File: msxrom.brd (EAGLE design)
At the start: 100 x 80 mm, 9 parts

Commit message: with io breakout
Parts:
- added JP10, JP11, JP12, JP13, JP15, JP16: (no value), pinhead-round:1X01
- added JP14, JP17, JP18, JP9: (no value), pinhead-round:1X04
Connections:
- new net !IORQ: JP1./IORQ, JP11.1
- new net !RD: JP1./RD, JP13.1, JP16.1
- new net !WAIT: JP1./WAIT, JP10.1
- new net !WR: JP1./WR, JP12.1, JP15.1
- new net N$9: JP1.SW1, JP1.SW2
- net A0: now also JP17.1
- net A1: now also JP17.2
- net A2: now also JP17.3
- net N$1: now also JP9.1
- net N$13: now also JP18.4
- net N$14: now also JP18.3
- net N$15: now also JP18.2
- net N$16: now also JP18.1
- net N$17: now also JP17.4
- net N$2: now also JP9.2
- net N$3: now also JP9.3
- net N$4: now also JP9.4
- net N$5: now also JP14.1
- net N$6: now also JP14.2
- net N$7: now also JP14.3
- net N$8: now also JP14.4
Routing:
- net !WR: track 0.00 -> 105.7 mm, vias 0 -> 3
- net !RD: track 0.00 -> 104.4 mm, vias 0 -> 2
- net !IORQ: track 0.00 -> 103.4 mm, vias 0 -> 2
- net !WAIT: track 0.00 -> 74.0 mm, vias 0 -> 2
- net N$13: track 45.0 -> 91.7 mm, vias 1 -> 2
- net N$14: track 55.1 -> 98.6 mm, vias 4 -> 5
- net N$15: track 54.4 -> 94.7 mm, vias 3 -> 4
- net N$16: track 50.1 -> 87.1 mm, vias 2 -> 3
- net N$17: track 46.8 -> 81.5 mm, vias 3 -> 4
- net A2: track 42.4 -> 75.2 mm, vias 2 -> 3
- net A1: track 39.2 -> 70.1 mm, vias 1 -> 2
- net N$1: track 39.9 -> 70.4 mm, vias 2 -> 4
- net N$4: track 27.2 -> 56.9 mm
- net N$6: track 27.2 -> 56.9 mm
- net N$5: track 22.9 -> 52.6 mm
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- added copper zone on layer 16, net GND

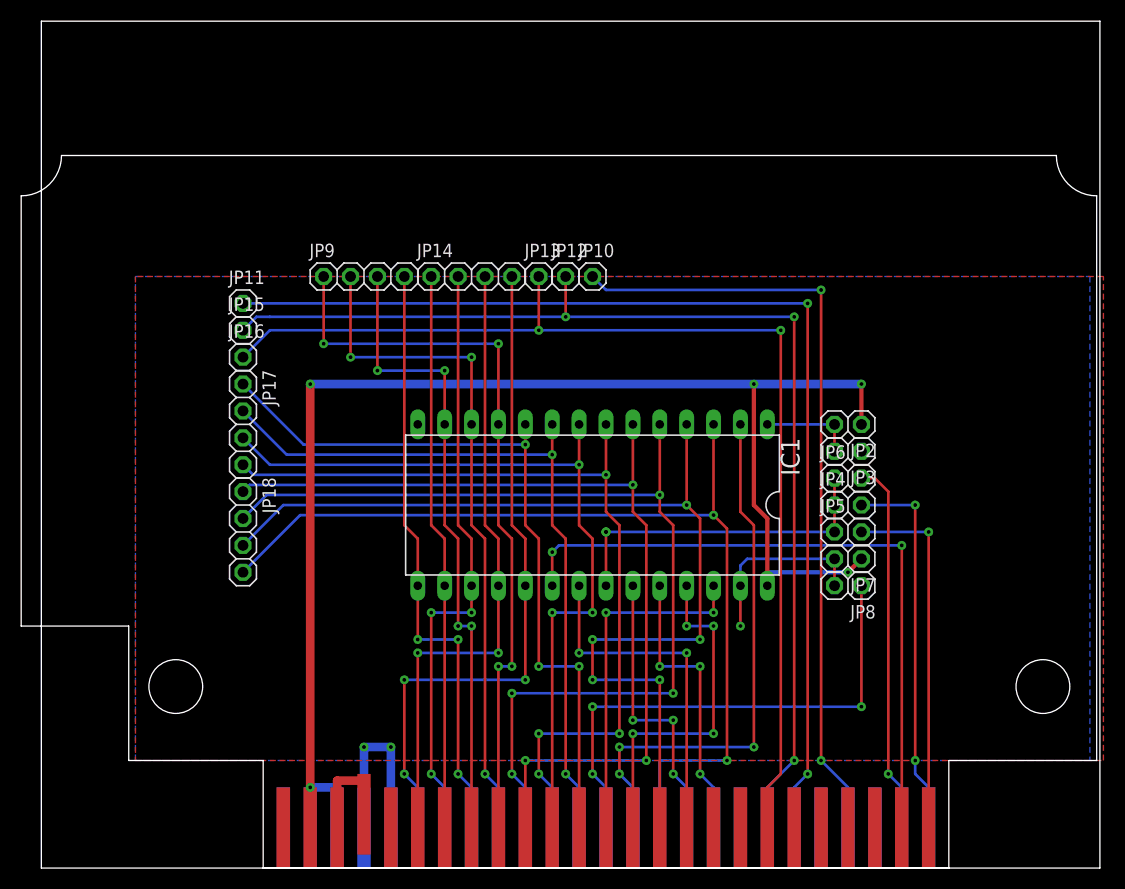
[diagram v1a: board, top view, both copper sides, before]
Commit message: finished board but eagle broke something...
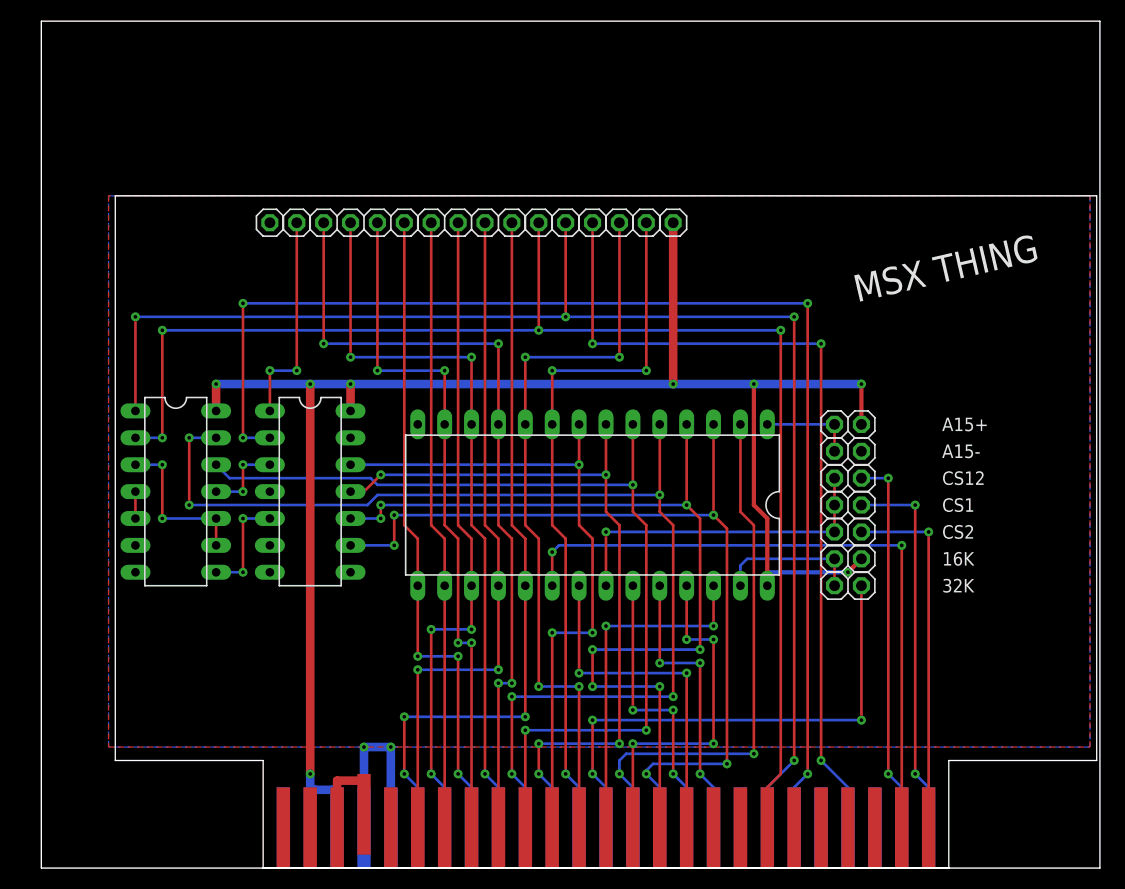
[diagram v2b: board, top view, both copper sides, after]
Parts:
- removed JP11, JP15, JP16: (no value), pinhead-round:1X01
- removed JP17, JP18: (no value), pinhead-round:1X04
- added A15+, A15-, CS1, CS12, CS2: (no value), pinhead-round:1X02
- added V1: 74HCT00N, 74ttl-din:DIL14
- added V2: 744078N, 74ttl-din:DIL14
- JP2, JP3, JP4, JP5, JP6: device pinhead-round:1X02 -> pinhead-round:1X01
- moved JP5 61.9 mm to (21.6, 61.0)
- moved JP2 55.4 mm to (24.1, 61.0), turned to 0 degrees
- moved JP4 32.8 mm to (57.1, 61.0)
- moved JP3 30.5 mm to (54.6, 61.0), turned to 0 degrees
- moved JP6 29.2 mm to (59.7, 61.0)
- moved JP10 5.08 mm to (52.1, 61.0)
- moved JP12 5.08 mm to (49.5, 61.0)
- moved JP13 5.08 mm to (47.0, 61.0)
- moved JP14 5.08 mm to (40.6, 61.0)
- moved JP9 5.08 mm to (30.5, 61.0)
- renumbered JP7 to 16K, JP8 to 32K
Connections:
- removed net N$13: IC1.3, JP1.A7, JP18.4
- removed net N$14: IC1.4, JP1.A6, JP18.3
- removed net N$15: IC1.5, JP1.A5, JP18.2
- removed net N$16: IC1.6, JP1.A4, JP18.1
- removed net N$17: IC1.7, JP1.A3, JP17.4
- new net !A4A5: V1.11, V2.3
- new net !IOSEL: JP2.1, V2.1
- new net !RW: V1.8, V2.5
- new net A3: IC1.7, JP1.A3, V2.11
- new net A4: IC1.6, JP1.A4, V1.12
- new net A5: IC1.5, JP1.A5, V1.13
- new net A6: IC1.4, JP1.A6, V2.10
- new net A7: IC1.3, JP1.A7, V2.9
- new net N$10: V1.10, V1.3, V1.9
- net !CS1: now also CS1.2; no longer JP4.2
- net !CS12: now also CS12.2; no longer JP6.2
- net !CS2: now also CS2.2; no longer JP5.2
- net !IORQ: now also V2.2; no longer JP11.1
- net !OE: now also CS1.1, CS12.1, CS2.1; no longer JP4.1, JP5.1, JP6.1
- net !RD: now also V1.2; no longer JP16.1
- net !WR: now also V1.1; no longer JP15.1
- net A0: now also JP3.1; no longer JP17.1
- net A1: now also JP4.1; no longer JP17.2
- net A15: now also A15+.2, A15-.2; no longer JP2.2, JP3.2
- net A2: now also V2.12; no longer JP17.3
- net GND: now also A15-.1, JP5.1, V1.4, V1.5, V1.7, V2.4, V2.7; no longer JP3.1
- net VCC: now also A15+.1, JP6.1, V1.14, V2.14; no longer JP2.1
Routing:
- net A5: track 0.00 -> 108.1 mm, vias 0 -> 6
- net N$14: track 98.6 -> 0.00 mm, vias 5 -> 0
- net N$15: track 94.7 -> 0.00 mm, vias 4 -> 0
- net N$13: track 91.7 -> 0.00 mm, vias 2 -> 0
- net A4: track 0.00 -> 90.2 mm, vias 0 -> 3
- net A6: track 0.00 -> 88.2 mm, vias 0 -> 7
- net N$16: track 87.1 -> 0.00 mm, vias 3 -> 0
- net A7: track 0.00 -> 83.5 mm, vias 0 -> 5
- net N$17: track 81.5 -> 0.00 mm, vias 4 -> 0
- net A3: track 0.00 -> 71.6 mm, vias 0 -> 5
- net VCC: track 134.4 -> 167.3 mm, vias 5 -> 8
- net !RD: track 104.4 -> 128.8 mm, vias 2 -> 4
- net !WR: track 105.7 -> 129.3 mm, vias 3 -> 4
- net !IOSEL: track 0.00 -> 20.3 mm, vias 0 -> 2
- net !IORQ: track 103.4 -> 118.6 mm, vias 2 -> 4
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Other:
- board text added: "MSX THING"

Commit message: with sdx connector and branding
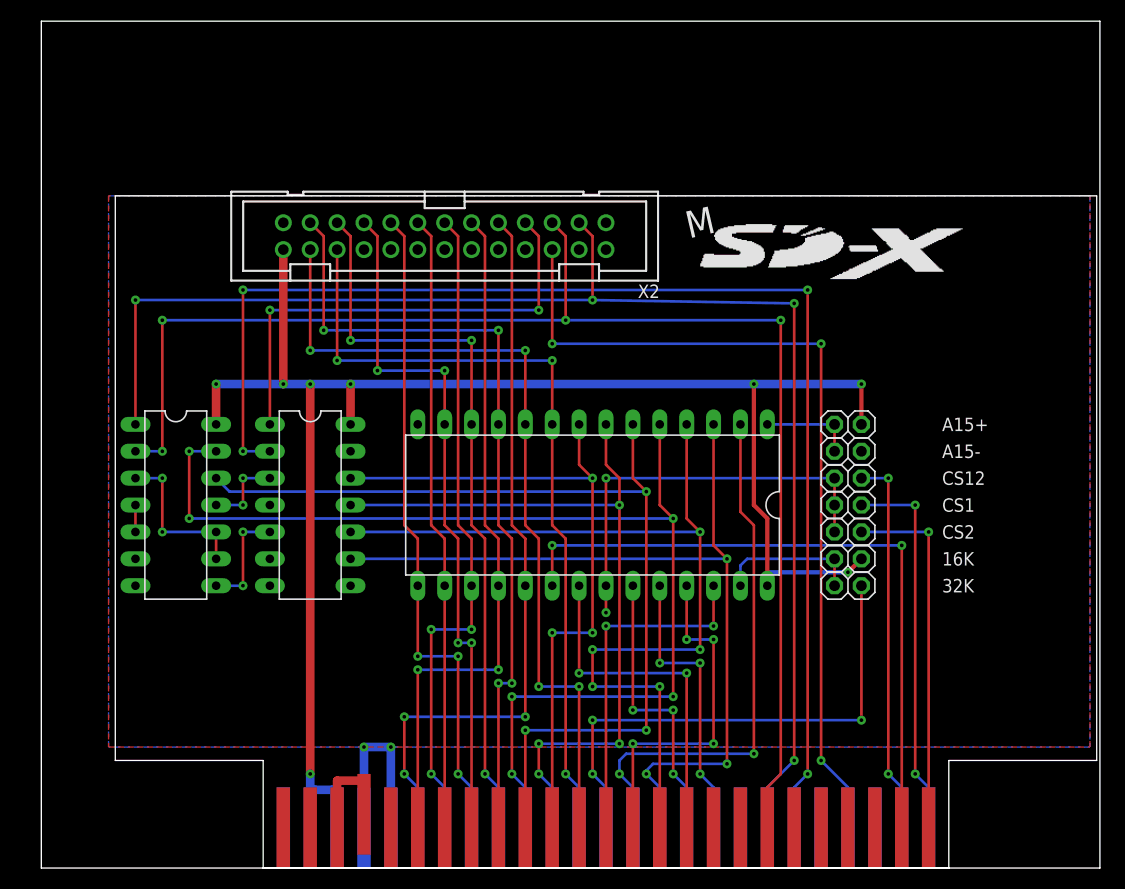
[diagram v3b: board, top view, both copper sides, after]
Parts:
- removed JP10, JP12, JP13, JP2, JP3, JP4, JP5, JP6: (no value), pinhead-round:1X01
- removed JP14, JP9: (no value), pinhead-round:1X04
- added X2: 2526-, con-3m:PAK100/2500-26
- moved V1 1.27 mm to (12.7, 34.3)
- moved V2 1.27 mm to (25.4, 34.3)
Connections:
- removed net N$1: IC1.11, JP1.D0, JP9.1
- removed net N$2: IC1.12, JP1.D1, JP9.2
- removed net N$3: IC1.13, JP1.D2, JP9.3
- removed net N$4: IC1.15, JP1.D3, JP9.4
- removed net N$5: IC1.16, JP1.D4, JP14.1
- removed net N$6: IC1.17, JP1.D5, JP14.2
- removed net N$7: IC1.18, JP1.D6, JP14.3
- removed net N$8: IC1.19, JP1.D7, JP14.4
- new net !RESET: X2.8
- new net D0: IC1.11, JP1.D0, X2.23
- new net D1: IC1.12, JP1.D1, X2.21
- new net D2: IC1.13, JP1.D2, X2.19
- new net D3: IC1.15, JP1.D3, X2.17
- new net D4: IC1.16, JP1.D4, X2.15
- new net D5: IC1.17, JP1.D5, X2.13
- new net D6: IC1.18, JP1.D6, X2.11
- new net D7: IC1.19, JP1.D7, X2.9
- new net RX-S: X2.4
- new net TX-S: X2.2
- net !IOSEL: now also X2.7; no longer JP2.1
- net !RD: now also X2.5; no longer JP13.1
- net !WAIT: now also X2.6; no longer JP10.1
- net !WR: now also X2.3; no longer JP12.1
- net A0: now also X2.24; no longer JP3.1
- net A1: now also X2.22; no longer JP4.1
- net GND: now also X2.1; no longer JP5.1
- net VCC: now also X2.26; no longer JP6.1
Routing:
- net D0: track 0.00 -> 76.0 mm, vias 0 -> 4
- net N$1: track 75.5 -> 0.00 mm, vias 4 -> 0
- net D7: track 0.00 -> 70.2 mm, vias 0 -> 3
- net D1: track 0.00 -> 70.2 mm, vias 0 -> 3
- net N$2: track 69.6 -> 0.00 mm, vias 3 -> 0
- net N$8: track 69.6 -> 0.00 mm, vias 3 -> 0
- net D6: track 0.00 -> 65.8 mm, vias 0 -> 2
- net D2: track 0.00 -> 65.8 mm, vias 0 -> 4
- net N$3: track 65.3 -> 0.00 mm, vias 4 -> 0
- net N$7: track 65.3 -> 0.00 mm, vias 2 -> 0
- net D5: track 0.00 -> 62.5 mm, vias 0 -> 3
- net D3: track 0.00 -> 62.5 mm, vias 0 -> 3
- net N$6: track 62.0 -> 0.00 mm, vias 3 -> 0
- net N$4: track 62.0 -> 0.00 mm, vias 3 -> 0
- net D4: track 0.00 -> 58.2 mm
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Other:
- board text added: "M"
- board text removed: "MSX THING"

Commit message: msxrom as produced
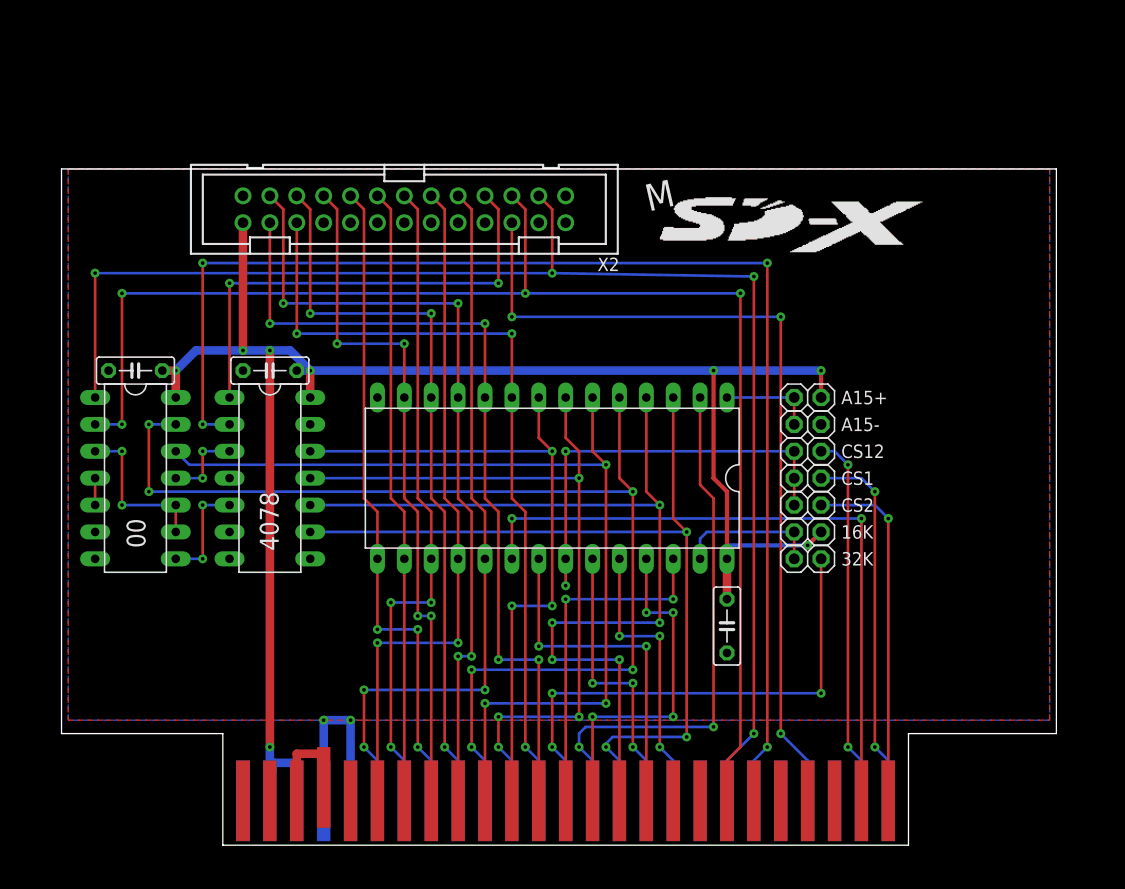
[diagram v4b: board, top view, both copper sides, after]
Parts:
- added C1, C2, C3: (no value), rcl:C050-025X075
- moved A15+ 4.58 mm to (72.4, 44.5)
- moved 16K 4.58 mm to (72.4, 31.8)
- moved 32K 4.58 mm to (72.4, 29.2)
- moved A15- 4.58 mm to (72.4, 41.9)
- moved CS1 4.58 mm to (72.4, 36.8)
- moved CS12 4.58 mm to (72.4, 39.4)
- moved CS2 4.58 mm to (72.4, 34.3)
- moved IC1 4.58 mm to (48.3, 36.8)
- moved JP1 4.58 mm to (45.7, 43.2)
- moved X2 4.58 mm to (34.3, 62.2)
- moved V1 4.58 mm to (8.89, 36.8)
- moved V2 4.58 mm to (21.6, 36.8)
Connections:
- net GND: now also C1.2, C2.2, C3.2
- net VCC: now also C1.1, C2.1, C3.1
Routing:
- net VCC: track 167.3 -> 170.1 mm
- net !CS12: track 36.1 -> 35.3 mm
- net !CS2: track 34.3 -> 33.5 mm
- net !CS1: track 36.1 -> 35.3 mm
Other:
- board size 100 x 80 mm -> 94 x 63.9 mm
- board text added: "00"
- board text added: "4078"

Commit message: loose files
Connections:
- removed net !IOSEL: V2.1, X2.7
- new net IOSEL: V2.13, X2.7
- net !RESET: now also JP1./RESET
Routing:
- net !RESET: track 0.00 -> 112.3 mm, vias 0 -> 5
- net !IOSEL: track 45.0 -> 0.00 mm, vias 2 -> 0
- net IOSEL: track 0.00 -> 40.9 mm, vias 0 -> 2
- net !OE: track 39.4 -> 36.8 mm, vias 2 -> 1
- net VCC: vias 8 -> 6
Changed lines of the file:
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@@
 <contactref element="V2" pad="14"/>
 <wire x1="21.59" y1="48.895" x2="19.05" y2="48.895" width="0.8128" layer="16"/>
-<via x="12.7" y="46.99" extent="1-16" drill="0.35"/>
 <wire x1="19.05" y1="48.895" x2="14.605" y2="48.895" width="0.8128" layer="16"/>
 <wire x1="14.605" y1="48.895" x2="12.7" y2="46.99" width="0.8128" layer="16"/>
-<wire x1="12.7" y1="46.99" x2="12.7" y2="44.45" width="0.8128" layer="1"/>
-<wire x1="25.4" y1="44.45" x2="25.4" y2="46.99" width="0.8128" layer="1"/>
-<via x="25.4" y="46.99" extent="1-16" drill="0.35"/>
+<wire x1="12.7" y1="46.99" x2="12.7" y2="44.45" width="0.8128" layer="16"/>
+<wire x1="25.4" y1="44.45" x2="25.4" y2="46.99" width="0.8128" layer="16"/>
 <via x="21.59" y="11.43" extent="1-16" drill="0.35"/>
 <wire x1="24.13" y1="6.35" x2="23.9014" y2="6.1214" width="0.8128" layer="16"/>
@@
 <contactref element="C3" pad="1"/>
 <wire x1="64.77" y1="29.21" x2="64.77" y2="25.4" width="0.8128" layer="1"/>
-<wire x1="11.43" y1="46.99" x2="12.7" y2="46.99" width="0.8128" layer="1"/>
+<wire x1="11.43" y1="46.99" x2="12.7" y2="46.99" width="0.8128" layer="16"/>
 <wire x1="24.13" y1="46.99" x2="25.4" y2="46.99" width="0.8128" layer="16"/>
 </signal>
@@
 <contactref element="CS2" pad="1"/>
 <contactref element="CS12" pad="1"/>
-<wire x1="49.53" y1="29.21" x2="49.53" y2="26.67" width="0.254" layer="1"/>
-<via x="49.53" y="26.67" extent="1-16" drill="0.35"/>
 <wire x1="49.53" y1="29.21" x2="49.53" y2="39.37" width="0.254" layer="1"/>
 <via x="49.53" y="39.37" extent="1-16" drill="0.35"/>
@@
 <via x="60.96" y="12.3825" extent="1-16" drill="0.35"/>
 <contactref element="V2" pad="9"/>
-<wire x1="60.96" y1="31.75" x2="60.96" y2="12.3825" width="0.254" layer="1"/>
+<wire x1="60.96" y1="31.75" x2="60.96" y2="29.21" width="0.254" layer="1"/>
 <via x="53.34" y="11.43" extent="1-16" drill="0.35"/>
 <via x="60.96" y="31.75" extent="1-16" drill="0.35"/>
+<wire x1="60.96" y1="29.21" x2="60.96" y2="12.3825" width="0.254" layer="1"/>
 <wire x1="25.4" y1="31.75" x2="60.96" y2="31.75" width="0.254" layer="16"/>
 </signal>
@@
 <wire x1="15.24" y1="36.83" x2="12.7" y2="36.83" width="0.254" layer="16"/>
 </signal>
-<signal name="!IOSEL">
-<contactref element="V2" pad="1"/>
-<via x="43.18" y="55.245" extent="1-16" drill="0.35"/>
-<wire x1="43.18" y1="55.245" x2="17.78" y2="55.245" width="0.254" layer="16"/>
-<via x="17.78" y="55.245" extent="1-16" drill="0.35"/>
-<wire x1="17.78" y1="55.245" x2="17.78" y2="44.45" width="0.254" layer="1"/>
-<contactref element="X2" pad="7"/>
-<wire x1="43.18" y1="55.245" x2="43.18" y2="62.23" width="0.254" layer="1"/>
-<wire x1="43.18" y1="62.23" x2="41.91" y2="63.5" width="0.254" layer="1"/>
-</signal>
 <signal name="D0">
 <contactref element="X2" pad="23"/>
@@
 <signal name="!RESET">
 <contactref element="X2" pad="8"/>
+<contactref element="JP1" pad="/RESET"/>
+<wire x1="62.23" y1="6.35" x2="62.23" y2="11.43" width="0.254" layer="16"/>
+<via x="62.23" y="11.43" extent="1-16" drill="0.35"/>
+<wire x1="62.23" y1="11.43" x2="62.23" y2="26.67" width="0.254" layer="1"/>
+<via x="62.23" y="26.67" extent="1-16" drill="0.35"/>
+<wire x1="62.23" y1="26.67" x2="81.28" y2="26.67" width="0.254" layer="16"/>
+<via x="81.28" y="26.67" extent="1-16" drill="0.35"/>
+<wire x1="81.28" y1="26.67" x2="81.28" y2="49.53" width="0.254" layer="1"/>
+<via x="81.28" y="49.53" extent="1-16" drill="0.35"/>
+<wire x1="81.28" y1="49.53" x2="43.18" y2="49.53" width="0.254" layer="16"/>
+<via x="43.18" y="49.53" extent="1-16" drill="0.35"/>
+<wire x1="43.18" y1="49.53" x2="43.18" y2="52.07" width="0.254" layer="1"/>
+<wire x1="43.18" y1="52.07" x2="41.91" y2="53.34" width="0.254" layer="1"/>
+<wire x1="41.91" y1="53.34" x2="41.91" y2="60.96" width="0.254" layer="1"/>
 </signal>
 <signal name="D3">
@@
 <contactref element="X2" pad="4"/>
 </signal>
+<signal name="IOSEL">
+<contactref element="V2" pad="13"/>
+<via x="43.18" y="55.245" extent="1-16" drill="0.35"/>
+<wire x1="43.18" y1="55.245" x2="26.67" y2="55.245" width="0.254" layer="16"/>
+<via x="26.67" y="55.245" extent="1-16" drill="0.35"/>
+<contactref element="X2" pad="7"/>
+<wire x1="43.18" y1="55.245" x2="43.18" y2="62.23" width="0.254" layer="1"/>
+<wire x1="43.18" y1="62.23" x2="41.91" y2="63.5" width="0.254" layer="1"/>
+<wire x1="26.67" y1="55.245" x2="26.67" y2="46.99" width="0.1524" layer="1"/>
+<wire x1="26.67" y1="46.99" x2="27.94" y2="45.72" width="0.1524" layer="1"/>
+<wire x1="27.94" y1="45.72" x2="27.94" y2="43.18" width="0.1524" layer="1"/>
+<wire x1="27.94" y1="43.18" x2="26.67" y2="41.91" width="0.1524" layer="1"/>
+<wire x1="26.67" y1="41.91" x2="25.4" y2="41.91" width="0.1524" layer="1"/>
+</signal>
 </signals>
